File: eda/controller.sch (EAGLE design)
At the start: 66 parts, among them U1 STM32F405/7R, U2 ISL83491SOIC, U3 ISL83491SOIC, U4 ISL83491SOIC, U5 ISL83491SOIC, U6 LM3525, X1 MICROSD-SOCKETAMPHENOL, Y1 8 MHz/C_L=15 pF

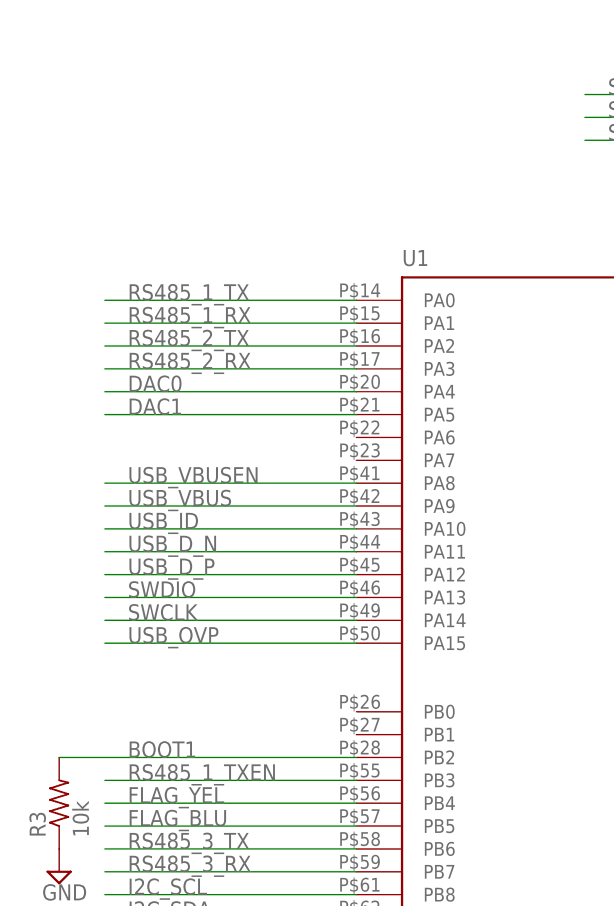
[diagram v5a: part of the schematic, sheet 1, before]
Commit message: Added ADC pins to a header just in case
In the future, a pseudo-battery-buzzer might be connected to them

Change-Id: I474a3178ecb004f360110c3845324daa48cb8223
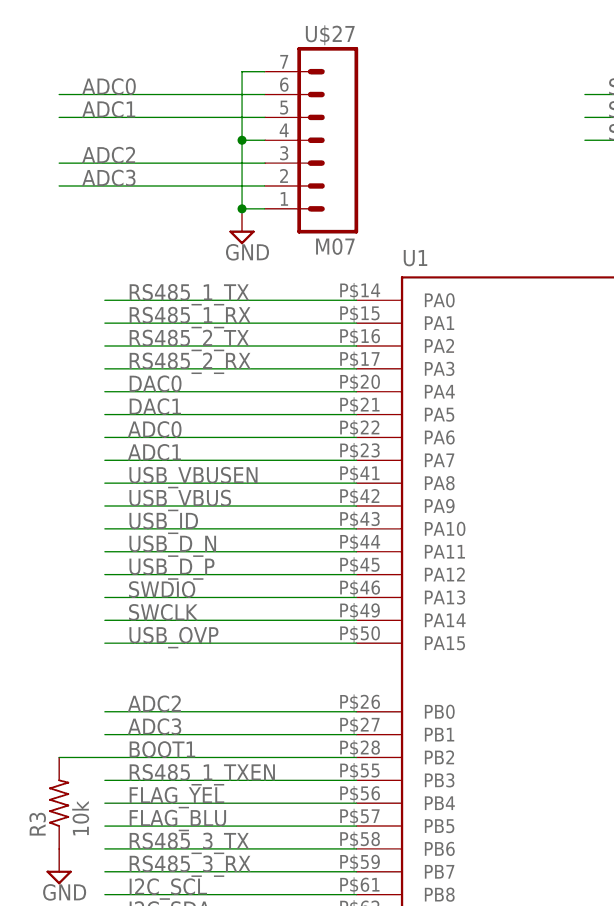
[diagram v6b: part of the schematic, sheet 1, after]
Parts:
- added U$27: M07, pie:M07
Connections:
- new net ADC0: U$27.6, U1.PA6
- new net ADC1: U$27.5, U1.PA7
- new net ADC2: U$27.3, U1.PB0
- new net ADC3: U$27.2, U1.PB1
- net GND: now also U$27.1, U$27.4, U$27.7
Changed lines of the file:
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@@
 <part name="SUPPLY31" library="pie" deviceset="GND" device=""/>
 <part name="SUPPLY32" library="pie" deviceset="GND" device=""/>
+<part name="U$27" library="pie" deviceset="M07" device=""/>
+<part name="SUPPLY33" library="pie" deviceset="GND" device=""/>
 </parts>
 <sheets>
@@
 <instance part="SUPPLY31" gate="GND" x="152.4" y="116.84"/>
 <instance part="SUPPLY32" gate="GND" x="86.36" y="162.56"/>
+<instance part="U$27" gate="G$1" x="38.1" y="170.18" rot="MR0"/>
+<instance part="SUPPLY33" gate="GND" x="27.94" y="160.02"/>
 </instances>
 <busses>
@@
 <wire x1="154.94" y1="121.92" x2="152.4" y2="121.92" width="0.1524" layer="91"/>
 <wire x1="152.4" y1="121.92" x2="152.4" y2="119.38" width="0.1524" layer="91"/>
+</segment>
+<segment>
+<pinref part="U$27" gate="G$1" pin="1"/>
+<pinref part="SUPPLY33" gate="GND" pin="GND"/>
+<wire x1="30.48" y1="162.56" x2="27.94" y2="162.56" width="0.1524" layer="91"/>
+<pinref part="U$27" gate="G$1" pin="4"/>
+<wire x1="30.48" y1="170.18" x2="27.94" y2="170.18" width="0.1524" layer="91"/>
+<wire x1="27.94" y1="170.18" x2="27.94" y2="162.56" width="0.1524" layer="91"/>
+<junction x="27.94" y="162.56"/>
+<pinref part="U$27" gate="G$1" pin="7"/>
+<wire x1="30.48" y1="177.8" x2="27.94" y2="177.8" width="0.1524" layer="91"/>
+<wire x1="27.94" y1="177.8" x2="27.94" y2="170.18" width="0.1524" layer="91"/>
+<junction x="27.94" y="170.18"/>
 </segment>
 </net>
@@
 </segment>
 </net>
+<net name="ADC0" class="0">
+<segment>
+<pinref part="U$27" gate="G$1" pin="6"/>
+<wire x1="30.48" y1="175.26" x2="7.62" y2="175.26" width="0.1524" layer="91"/>
+<label x="10.16" y="175.26" size="1.778" layer="95"/>
+</segment>
+<segment>
+<pinref part="U1" gate="G$1" pin="PA6"/>
+<wire x1="12.7" y1="137.16" x2="40.64" y2="137.16" width="0.1524" layer="91"/>
+<label x="15.24" y="137.16" size="1.778" layer="95"/>
+</segment>
+</net>
+<net name="ADC1" class="0">
+<segment>
+<pinref part="U$27" gate="G$1" pin="5"/>
+<wire x1="7.62" y1="172.72" x2="30.48" y2="172.72" width="0.1524" layer="91"/>
+<label x="10.16" y="172.72" size="1.778" layer="95"/>
+</segment>
+<segment>
+<pinref part="U1" gate="G$1" pin="PA7"/>
+<wire x1="12.7" y1="134.62" x2="40.64" y2="134.62" width="0.1524" layer="91"/>
+<label x="15.24" y="134.62" size="1.778" layer="95"/>
+</segment>
+</net>
+<net name="ADC2" class="0">
+<segment>
+<pinref part="U$27" gate="G$1" pin="3"/>
+<wire x1="7.62" y1="167.64" x2="30.48" y2="167.64" width="0.1524" layer="91"/>
+<label x="10.16" y="167.64" size="1.778" layer="95"/>
+</segment>
+<segment>
+<pinref part="U1" gate="G$1" pin="PB0"/>
+<wire x1="12.7" y1="106.68" x2="40.64" y2="106.68" width="0.1524" layer="91"/>
+<label x="15.24" y="106.68" size="1.778" layer="95"/>
+</segment>
+</net>
+<net name="ADC3" class="0">
+<segment>
+<pinref part="U$27" gate="G$1" pin="2"/>
+<wire x1="7.62" y1="165.1" x2="30.48" y2="165.1" width="0.1524" layer="91"/>
+<label x="10.16" y="165.1" size="1.778" layer="95"/>
+</segment>
+<segment>
+<pinref part="U1" gate="G$1" pin="PB1"/>
+<wire x1="12.7" y1="104.14" x2="40.64" y2="104.14" width="0.1524" layer="91"/>
+<label x="15.24" y="104.14" size="1.778" layer="95"/>
+</segment>
+</net>

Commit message: Add power supplies to controller board
Change-Id: Iaeb964f5bd3540551bfd9420b17e33929b5b7182
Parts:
- added C22, C23, C29, C30: 10 uF, pie:CAP0603-CAP
- added C24: 1 uF, pie:CAP0603-CAP
- added C25: 3.3 nF, pie:CAP0603-CAP
- added C26: 0.1 uF, pie:CAP0603-CAP
- added C27, C28: 22 uF, pie:CAP0603-CAP
- added L1: 4.7 uH, pie:INDUCTOR0603
- added R14: 22.1k, pie:R-US_R0603
- added R15: 124k, pie:R-US_R0603
- added R16: 10k, pie:R-US_R0603
- added U$28: XT60CONNECTOR, pie:XT60CONNECTOR
- added U$29: TPS54227DDA, pie:TPS54227DDA
- added U7: 3.3V, pie:LM1117
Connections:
- new net N$11: C22.1, C23.1, R16.2, U$28.12V, U$29.VIN
- new net N$12: C26.1, U$29.VBST
- new net N$13: C25.1, U$29.SS
- new net N$14: C24.1, U$29.VREG5
- new net N$15: R14.1, R15.2, U$29.VFB
- new net N$16: R16.1, U$29.EN
- new net N$17: C26.2, L1.1, U$29.SW
- net 3.3V: now also C29.1, U7.OUT
- net 5V: now also C27.1, C28.1, C30.1, L1.2, R14.2, U7.IN
- net GND: now also C22.2, C23.2, C24.2, C25.2, C27.2, C28.2, C29.2, C30.2, R15.1, U$28.GND, U$29.GND, U$29.GND_PAD, U7.GND
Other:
- note added: "Power supplies"
- note added: "TODO: Anderson conn"
- note added: "TODO: Possibly a "Power On" button"

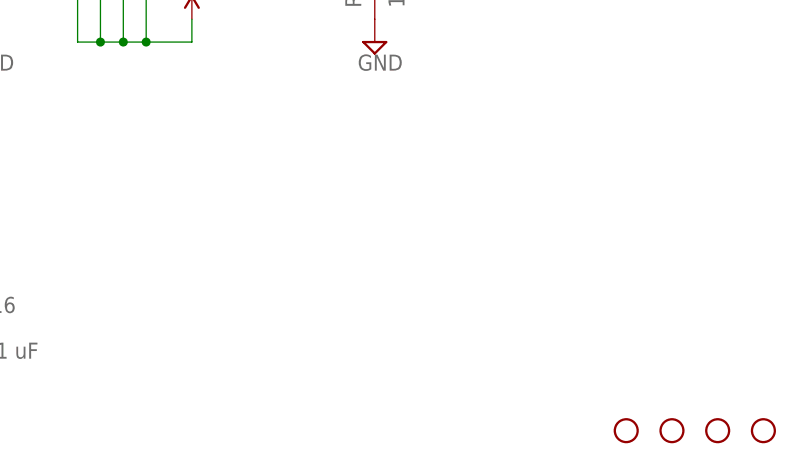
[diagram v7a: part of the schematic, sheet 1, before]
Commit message: Add reset button
Change-Id: I42acdf969c3e141ac8738e383c67deb6f76301bc
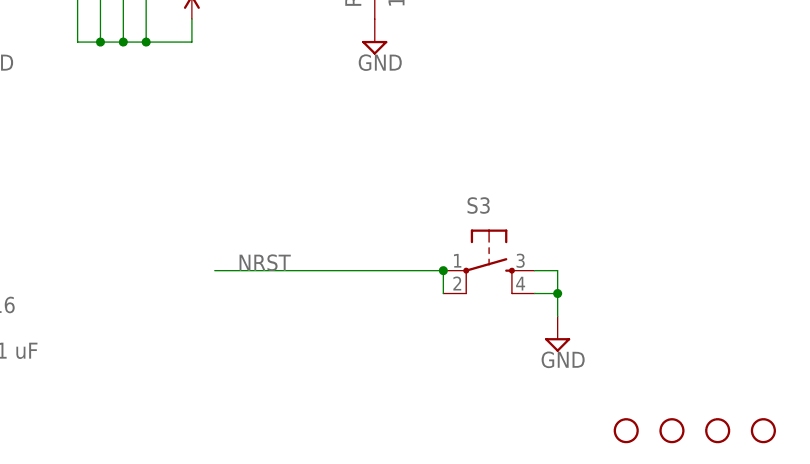
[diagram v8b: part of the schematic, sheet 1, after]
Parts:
- added S3: (no value), pie:TAC_SWITCHPTH
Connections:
- net GND: now also S3.3, S3.4
- net NRST: now also S3.1, S3.2
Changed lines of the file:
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@@
 <part name="C29" library="pie" deviceset="CAP" device="0603-CAP" value="10 uF"/>
 <part name="C30" library="pie" deviceset="CAP" device="0603-CAP" value="10 uF"/>
+<part name="S3" library="pie" deviceset="TAC_SWITCH" device="PTH"/>
+<part name="SUPPLY41" library="pie" deviceset="GND" device=""/>
 </parts>
 <sheets>
@@
 <instance part="U$27" gate="G$1" x="38.1" y="170.18" rot="MR0"/>
 <instance part="SUPPLY33" gate="GND" x="27.94" y="160.02"/>
+<instance part="S3" gate="S" x="114.3" y="20.32"/>
+<instance part="SUPPLY41" gate="GND" x="121.92" y="12.7"/>
 </instances>
 <busses>
@@
 <wire x1="27.94" y1="177.8" x2="27.94" y2="170.18" width="0.1524" layer="91"/>
 <junction x="27.94" y="170.18"/>
+</segment>
+<segment>
+<pinref part="S3" gate="S" pin="3"/>
+<pinref part="SUPPLY41" gate="GND" pin="GND"/>
+<wire x1="119.38" y1="20.32" x2="121.92" y2="20.32" width="0.1524" layer="91"/>
+<wire x1="121.92" y1="20.32" x2="121.92" y2="17.78" width="0.1524" layer="91"/>
+<pinref part="S3" gate="S" pin="4"/>
+<wire x1="121.92" y1="17.78" x2="121.92" y2="15.24" width="0.1524" layer="91"/>
+<wire x1="119.38" y1="17.78" x2="121.92" y2="17.78" width="0.1524" layer="91"/>
+<junction x="121.92" y="17.78"/>
 </segment>
 </net>
@@
 <label x="142.24" y="88.9" size="1.778" layer="95"/>
 </segment>
-</net>
+<segment>
+<pinref part="S3" gate="S" pin="1"/>
+<wire x1="109.22" y1="20.32" x2="83.82" y2="20.32" width="0.1524" layer="91"/>
+<pinref part="S3" gate="S" pin="2"/>
+<wire x1="109.22" y1="17.78" x2="109.22" y2="20.32" width="0.1524" layer="91"/>
+<junction x="109.22" y="20.32"/>
+<label x="86.36" y="20.32" size="1.778" layer="95"/>
+</segment>
+</net>
